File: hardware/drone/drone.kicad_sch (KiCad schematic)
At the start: 0 parts

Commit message: Finished STM32N6 schematic symbol
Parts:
- added U1: STM32N645I0, symbol SoftDrone:STM32N645I0

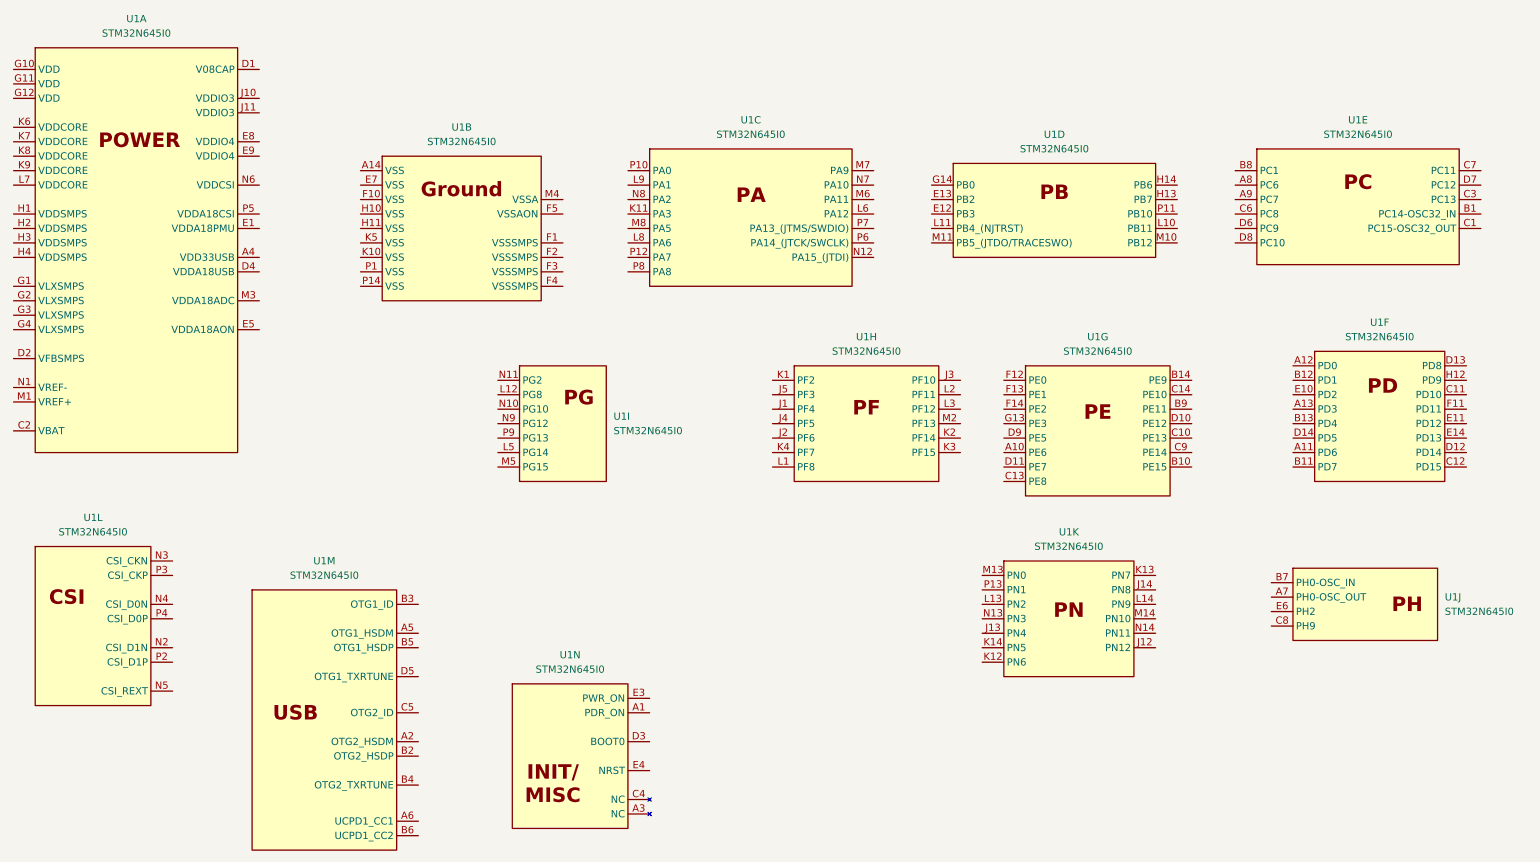
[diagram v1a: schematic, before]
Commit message: Continued project plan. Started PDN design
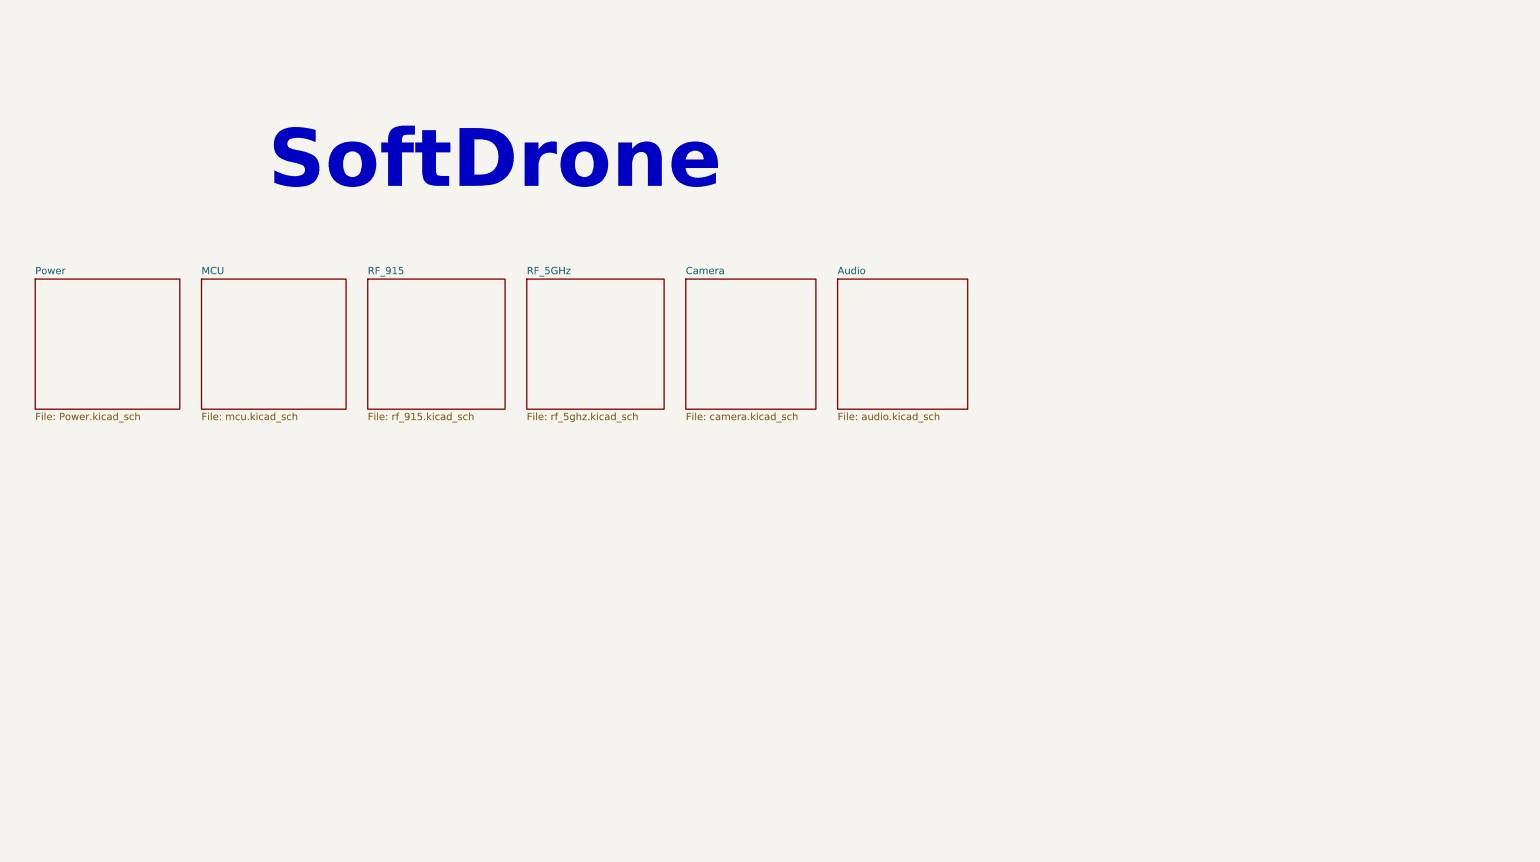
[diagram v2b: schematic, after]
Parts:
- removed U1: STM32N645I0, symbol SoftDrone:STM32N645I0
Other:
- added sheet Audio (audio.kicad_sch)
- added sheet Camera (camera.kicad_sch)
- added sheet MCU (mcu.kicad_sch)
- added sheet Power (Power.kicad_sch)
- added sheet RF_5GHz (rf_5ghz.kicad_sch)
- added sheet RF_915 (rf_915.kicad_sch)
- note added: "SoftDrone"

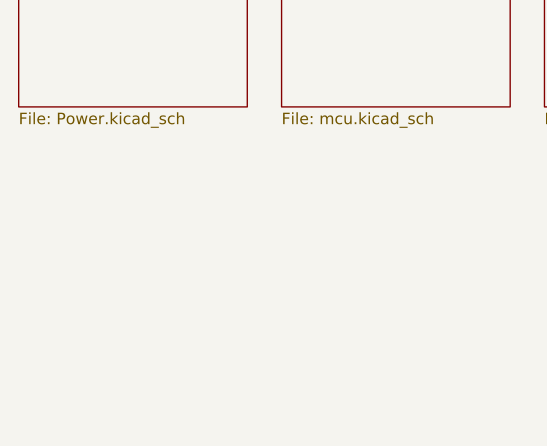
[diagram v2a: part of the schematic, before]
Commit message: Pinmuxxed codec and picked and completed IMU schematic
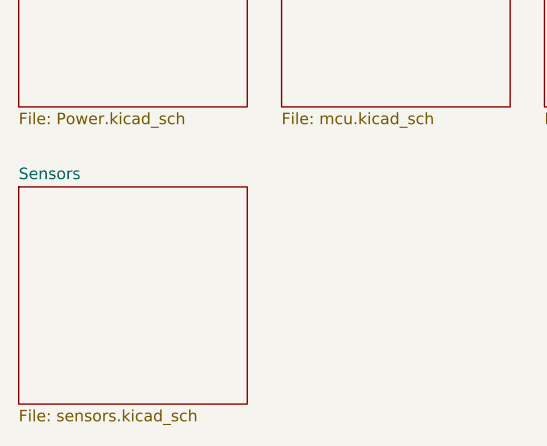
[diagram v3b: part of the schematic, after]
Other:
- added sheet Sensors (sensors.kicad_sch)
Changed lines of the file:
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@@
+	)
+	(sheet
+		(at 22.86 95.25)
+		(size 25.4 24.13)
+		(exclude_from_sim no)
+		(in_bom yes)
+		(on_board yes)
+		(dnp no)
+		(fields_autoplaced yes)
+		(stroke
+			(width 0.1524)
+			(type solid)
+		)
+		(fill
+			(color 0 0 0 0)
+		)
+		(property "Sheetname" "Sensors"
+			(at 22.86 94.5384 0)
+			(show_name no)
+			(do_not_autoplace no)
+			(effects
+				(font
+					(size 1.27 1.27)
+				)
+				(justify left bottom)
+			)
+		)
+		(property "Sheetfile" "sensors.kicad_sch"
+			(at 22.86 119.9646 0)
+			(show_name no)
+			(do_not_autoplace no)
+			(effects
+				(font
+					(size 1.27 1.27)
+				)
+				(justify left top)
+			)
+		)
+		(instances
+			(project "drone"
+				(path "/62c402a6-ed3f-446b-8423-821e9cc6908b"
+					(page "8")
+				)
+			)
+		)
 	)
 	(sheet

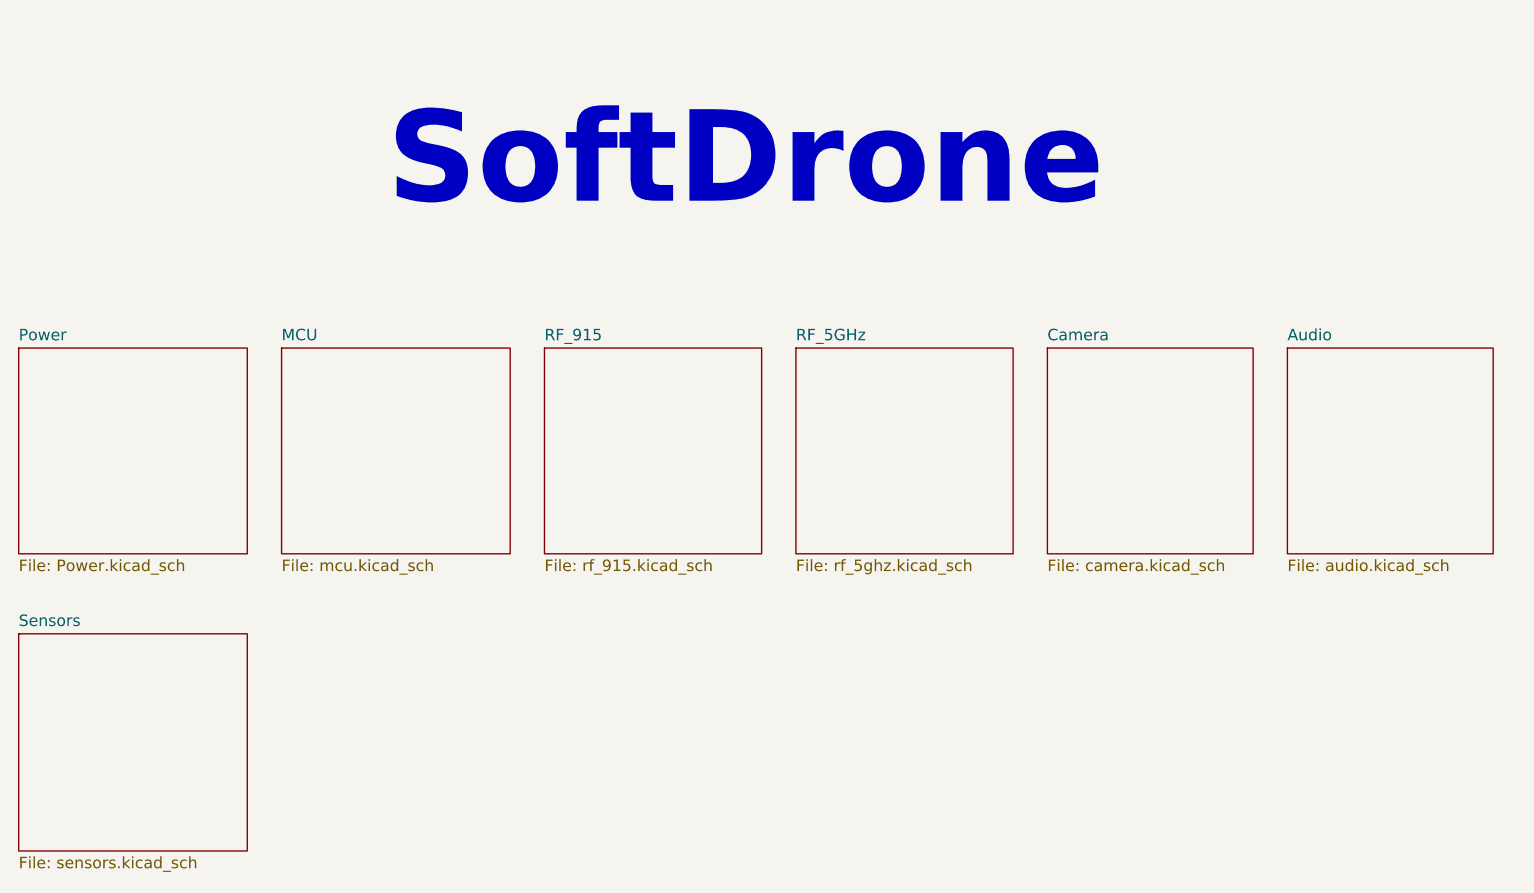
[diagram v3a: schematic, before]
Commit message: Added barometer, more pinmuxxing, added VBAT sensing and reverse voltage protection
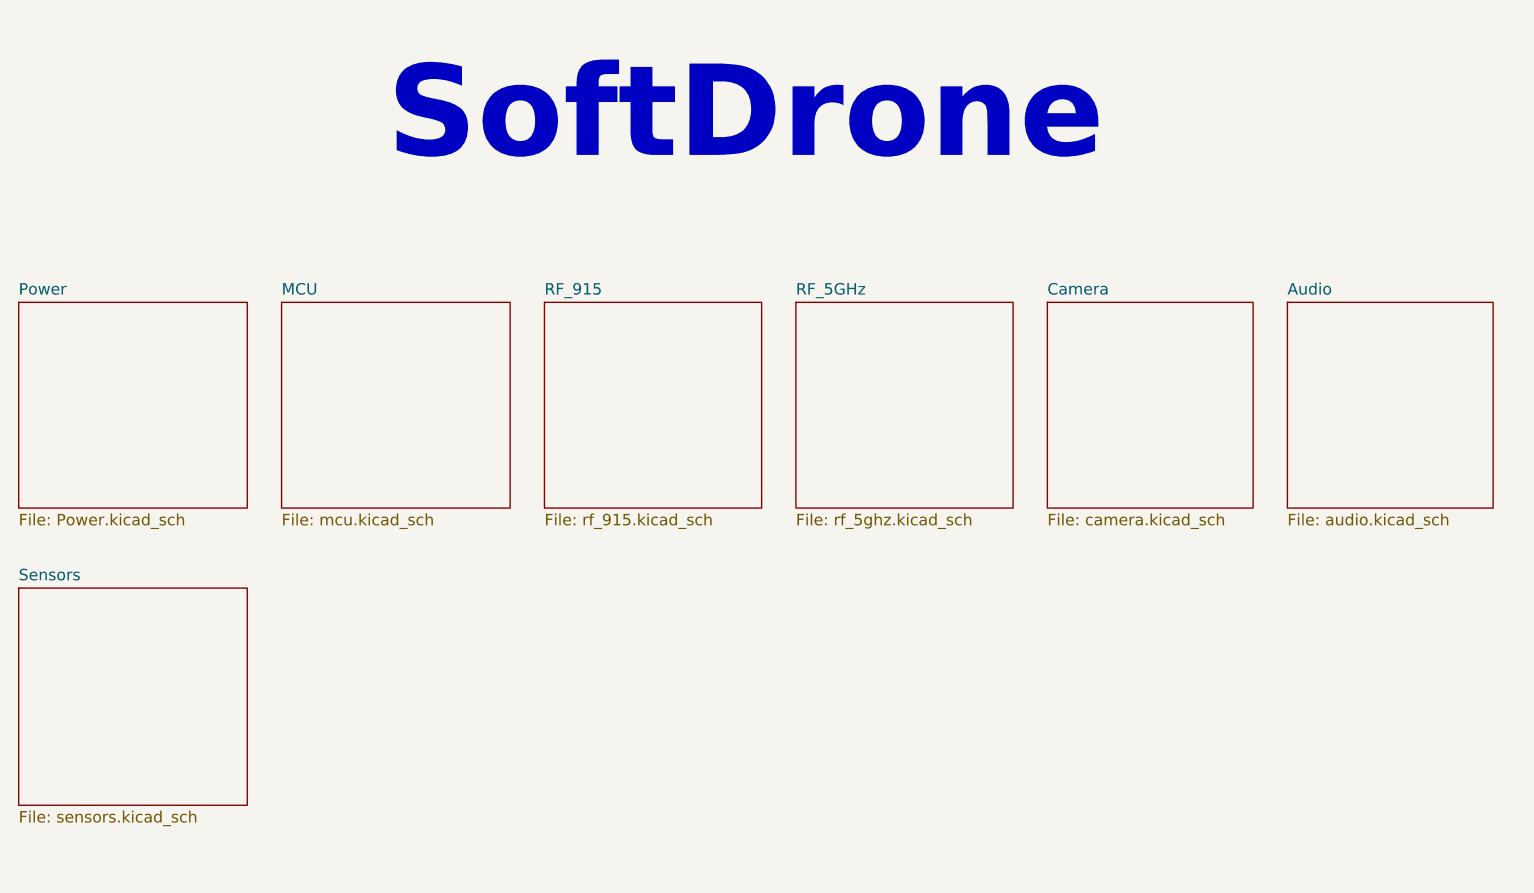
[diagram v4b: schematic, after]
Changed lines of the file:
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@@
 	(text "SoftDrone"
 		(exclude_from_sim no)
-		(at 103.632 42.672 0)
+		(at 103.632 37.592 0)
 		(effects
 			(font
@@
 	)
 	(sheet
-		(at 137.16 63.5)
+		(at 137.16 58.42)
 		(size 22.86 22.86)
 		(exclude_from_sim no)
@@
 		)
 		(property "Sheetname" "Camera"
-			(at 137.16 62.7884 0)
+			(at 137.16 57.7084 0)
 			(show_name no)
 			(do_not_autoplace no)
@@
 		)
 		(property "Sheetfile" "camera.kicad_sch"
-			(at 137.16 86.9446 0)
+			(at 137.16 81.8646 0)
 			(show_name no)
 			(do_not_autoplace no)
@@
 	)
 	(sheet
-		(at 109.22 63.5)
+		(at 109.22 58.42)
 		(size 24.13 22.86)
 		(exclude_from_sim no)
@@
 		)
 		(property "Sheetname" "RF_5GHz"
-			(at 109.22 62.7884 0)
+			(at 109.22 57.7084 0)
 			(show_name no)
 			(do_not_autoplace no)
@@
 		)
 		(property "Sheetfile" "rf_5ghz.kicad_sch"
-			(at 109.22 86.9446 0)
+			(at 109.22 81.8646 0)
 			(show_name no)
 			(do_not_autoplace no)
@@
 	)
 	(sheet
-		(at 81.28 63.5)
+		(at 81.28 58.42)
 		(size 24.13 22.86)
 		(exclude_from_sim no)
@@
 		)
 		(property "Sheetname" "RF_915"
-			(at 81.28 62.7884 0)
+			(at 81.28 57.7084 0)
 			(show_name no)
 			(do_not_autoplace no)
@@
 		)
 		(property "Sheetfile" "rf_915.kicad_sch"
-			(at 81.28 86.9446 0)
+			(at 81.28 81.8646 0)
 			(show_name no)
 			(do_not_autoplace no)
@@
 	)
 	(sheet
-		(at 22.86 95.25)
+		(at 22.86 90.17)
 		(size 25.4 24.13)
 		(exclude_from_sim no)
@@
 		)
 		(property "Sheetname" "Sensors"
-			(at 22.86 94.5384 0)
+			(at 22.86 89.4584 0)
 			(show_name no)
 			(do_not_autoplace no)
@@
 		)
 		(property "Sheetfile" "sensors.kicad_sch"
-			(at 22.86 119.9646 0)
+			(at 22.86 114.8846 0)
 			(show_name no)
 			(do_not_autoplace no)
@@
 	)
 	(sheet
-		(at 52.07 63.5)
+		(at 52.07 58.42)
 		(size 25.4 22.86)
 		(exclude_from_sim no)
@@
 		)
 		(property "Sheetname" "MCU"
-			(at 52.07 62.7884 0)
+			(at 52.07 57.7084 0)
 			(show_name no)
 			(do_not_autoplace no)
@@
 		)
 		(property "Sheetfile" "mcu.kicad_sch"
-			(at 52.07 86.9446 0)
+			(at 52.07 81.8646 0)
 			(show_name no)
 			(do_not_autoplace no)
@@
 	)
 	(sheet
-		(at 22.86 63.5)
+		(at 22.86 58.42)
 		(size 25.4 22.86)
 		(exclude_from_sim no)
@@
 		)
 		(property "Sheetname" "Power"
-			(at 22.86 62.7884 0)
+			(at 22.86 57.7084 0)
 			(show_name no)
 			(do_not_autoplace no)
@@
 		)
 		(property "Sheetfile" "Power.kicad_sch"
-			(at 22.86 86.9446 0)
+			(at 22.86 81.8646 0)
 			(show_name no)
 			(do_not_autoplace no)
@@
 	)
 	(sheet
-		(at 163.83 63.5)
+		(at 163.83 58.42)
 		(size 22.86 22.86)
 		(exclude_from_sim no)
@@
 		)
 		(property "Sheetname" "Audio"
-			(at 163.83 62.7884 0)
+			(at 163.83 57.7084 0)
 			(show_name no)
 			(do_not_autoplace no)
@@
 		)
 		(property "Sheetfile" "audio.kicad_sch"
-			(at 163.83 86.9446 0)
-			(show_name no)
-			(do_not_autoplace no)
+			(at 163.83 81.8646 0)
+			(show_name no)
+			(do_not_autoplace no)

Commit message: Moved power and pinmux tables to their own hierarchical sheet
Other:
- added sheet DESIGN_SUMMARY (designsummary.kicad_sch)
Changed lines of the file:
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@@
+		)
+	)
+	(sheet
+		(at 52.07 90.17)
+		(size 25.4 24.13)
+		(exclude_from_sim no)
+		(in_bom yes)
+		(on_board yes)
+		(dnp no)
+		(fields_autoplaced yes)
+		(stroke
+			(width 0.1524)
+			(type solid)
+		)
+		(fill
+			(color 0 0 0 0)
+		)
+		(property "Sheetname" "DESIGN_SUMMARY"
+			(at 52.07 89.4584 0)
+			(show_name no)
+			(do_not_autoplace no)
+			(effects
+				(font
+					(size 1.27 1.27)
+				)
+				(justify left bottom)
+			)
+		)
+		(property "Sheetfile" "designsummary.kicad_sch"
+			(at 52.07 114.8846 0)
+			(show_name no)
+			(do_not_autoplace no)
+			(effects
+				(font
+					(size 1.27 1.27)
+				)
+				(justify left top)
+			)
+		)
+		(instances
+			(project "drone"
+				(path "/62c402a6-ed3f-446b-8423-821e9cc6908b"
+					(page "9")
+				)
+			)
 		)
 	)
